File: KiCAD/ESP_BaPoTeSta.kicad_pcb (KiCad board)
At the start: 2 copper layers, 31.8 x 49.5 mm, 23 parts, among them P1 Progr, P2 Battery, P3 Power, P4 Upload, P5 Config, U1 MCP1700-330, U2 ESP-12, U3 DS18B20, U4 DHT22

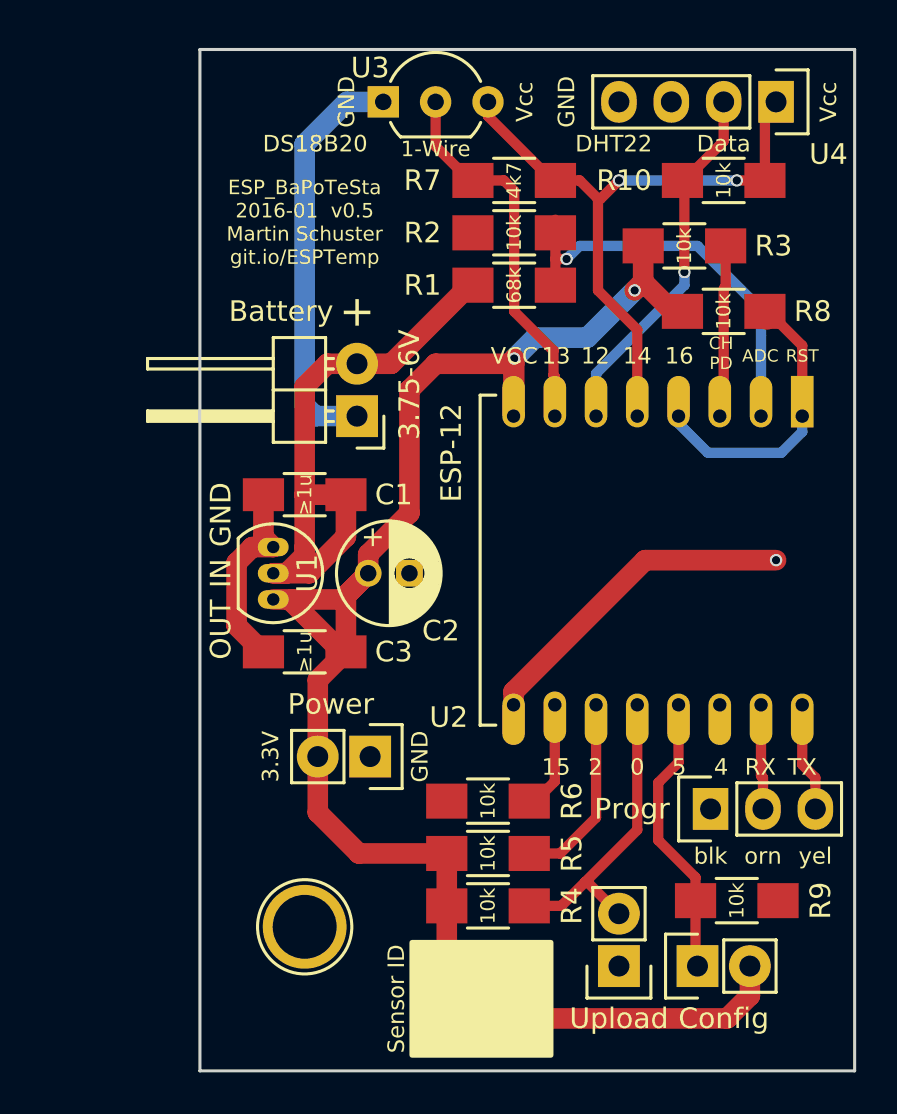
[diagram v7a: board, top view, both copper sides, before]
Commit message: ENH: [pcb] add strain relief for battery cable
and change type of 3mm-mounting-hole from "1pin" to "MountingHole"
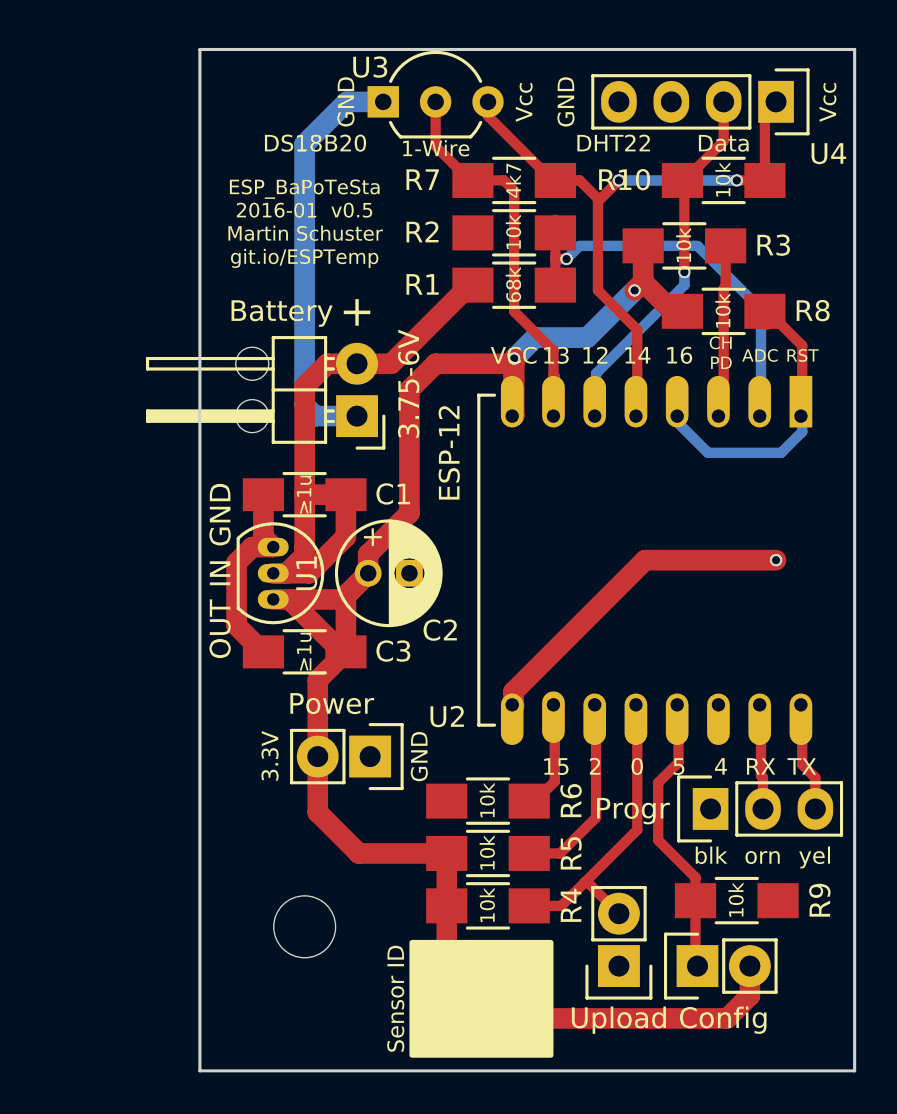
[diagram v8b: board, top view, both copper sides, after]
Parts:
- removed the REF** at (118.1, 108.6)
- added REF**: MountingHole_2-5mm, Mounting_Holes:MountingHole_2-5mm, F.Cu at (115.6, 83.8)
- added REF**: MountingHole_2-5mm, Mounting_Holes:MountingHole_2-5mm, F.Cu at (115.6, 81.3)
- added REF**: MountingHole_3mm, Mounting_Holes:MountingHole_3mm, F.Cu at (118.1, 108.6)
- moved U2 0.06 mm to (142.2, 83.8)
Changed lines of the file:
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@@
     (tracks 155)
     (zones 0)
-    (modules 23)
+    (modules 25)
     (nets 17)
   )
@@
     (mod_text_size 1 1)
     (mod_text_width 0.15)
-    (pad_size 1.4 1.4)
-    (pad_drill 1)
+    (pad_size 3 3)
+    (pad_drill 3)
     (pad_to_mask_clearance 0.2)
     (aux_axis_origin 113.03 66.04)
@@
     (add_net VCC)
   )
+  (module Mounting_Holes:MountingHole_2-5mm (layer F.Cu)
+    (at 115.57 83.82)
+    (descr "Mounting hole, Befestigungsbohrung, 2,5mm, No Annular, Kein Restring,")
+    (tags "Mounting hole, Befestigungsbohrung, 2,5mm, No Annular, Kein Restring,")
+    (fp_text reference REF** (at 0 -3.50012) (layer F.SilkS) hide
+      (effects (font (size 1 1) (thickness 0.15)))
+    )
+    (fp_text value MountingHole_2-5mm (at 0.09906 3.59918) (layer F.Fab)
+      (effects (font (size 1 1) (thickness 0.15)))
+    )
+    (fp_circle (center 0 0) (end 2.5 0) (layer Cmts.User) (width 0.381))
+    (pad "" np_thru_hole circle (at 0 0) (size 1.6 1.6) (drill 1.6) (layers *.Cu *.Mask F.SilkS))
+  )
   (module Capacitors_ThroughHole:C_Radial_D5_L11_P2 (layer F.Cu)
     (at 121.19 91.44)
@@
   )
   (module ESP8266:ESP-12 (layer F.Cu)
-    (at 142.24 83.82 270)
+    (at 142.175 83.82 270)
     (descr "Module, ESP-8266, ESP-12, 16 pad, SMD")
     (tags "Module ESP-8266 ESP8266")
@@
     )
   )
-  (module Connect:1pin (layer F.Cu)
-    (at 118.11 108.585)
-    (descr "module 1 pin (ou trou mecanique de percage)")
-    (tags DEV)
-    (fp_text reference REF** (at 0 -3.048) (layer F.SilkS) hide
-      (effects (font (size 1 1) (thickness 0.15)))
-    )
-    (fp_text value 1pin (at 0 2.794) (layer F.Fab) hide
-      (effects (font (size 1 1) (thickness 0.15)))
-    )
-    (fp_circle (center 0 0) (end 0 -2.286) (layer F.SilkS) (width 0.15))
-    (pad 1 thru_hole circle (at 0 0) (size 4.064 4.064) (drill 3.1) (layers *.Cu *.Mask F.SilkS))
-  )
   (module Capacitors_SMD:C_1206_HandSoldering (layer F.Cu)
     (at 118.11 87.63 180)
@@
     )
   )
+  (module Mounting_Holes:MountingHole_2-5mm (layer F.Cu)
+    (at 115.57 81.28)
+    (descr "Mounting hole, Befestigungsbohrung, 2,5mm, No Annular, Kein Restring,")
+    (tags "Mounting hole, Befestigungsbohrung, 2,5mm, No Annular, Kein Restring,")
+    (fp_text reference REF** (at 0 -3.50012) (layer F.SilkS) hide
+      (effects (font (size 1 1) (thickness 0.15)))
+    )
+    (fp_text value MountingHole_2-5mm (at 0.09906 3.59918) (layer F.Fab)
+      (effects (font (size 1 1) (thickness 0.15)))
+    )
+    (fp_circle (center 0 0) (end 2.5 0) (layer Cmts.User) (width 0.381))
+    (pad "" np_thru_hole circle (at 0 0) (size 1.6 1.6) (drill 1.6) (layers *.Cu *.Mask F.SilkS))
+  )
+  (module Mounting_Holes:MountingHole_3mm (layer F.Cu)
+    (at 118.11 108.585)
+    (descr "Mounting hole, Befestigungsbohrung, 3mm, No Annular, Kein Restring,")
+    (tags "Mounting hole, Befestigungsbohrung, 3mm, No Annular, Kein Restring,")
+    (fp_text reference REF** (at 0 -4.0005) (layer F.SilkS) hide
+      (effects (font (size 1 1) (thickness 0.15)))
+    )
+    (fp_text value MountingHole_3mm (at 1.00076 5.00126) (layer F.Fab)
+      (effects (font (size 1 1) (thickness 0.15)))
+    )
+    (fp_circle (center 0 0) (end 3 0) (layer Cmts.User) (width 0.381))
+    (pad "" np_thru_hole circle (at 0 0) (size 3 3) (drill 3) (layers *.Cu *.Mask F.SilkS))
+  )
   (gr_text Vcc (at 143.51 68.58 90) (layer F.SilkS)
